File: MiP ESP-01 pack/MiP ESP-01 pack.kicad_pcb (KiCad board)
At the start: 2 copper layers, 41.4 x 63.8 mm, 19 parts, among them J1 MiP, J2 Debug, U1 ESP-01, U2 74LVC1G125, U3 AMS1117-3.3

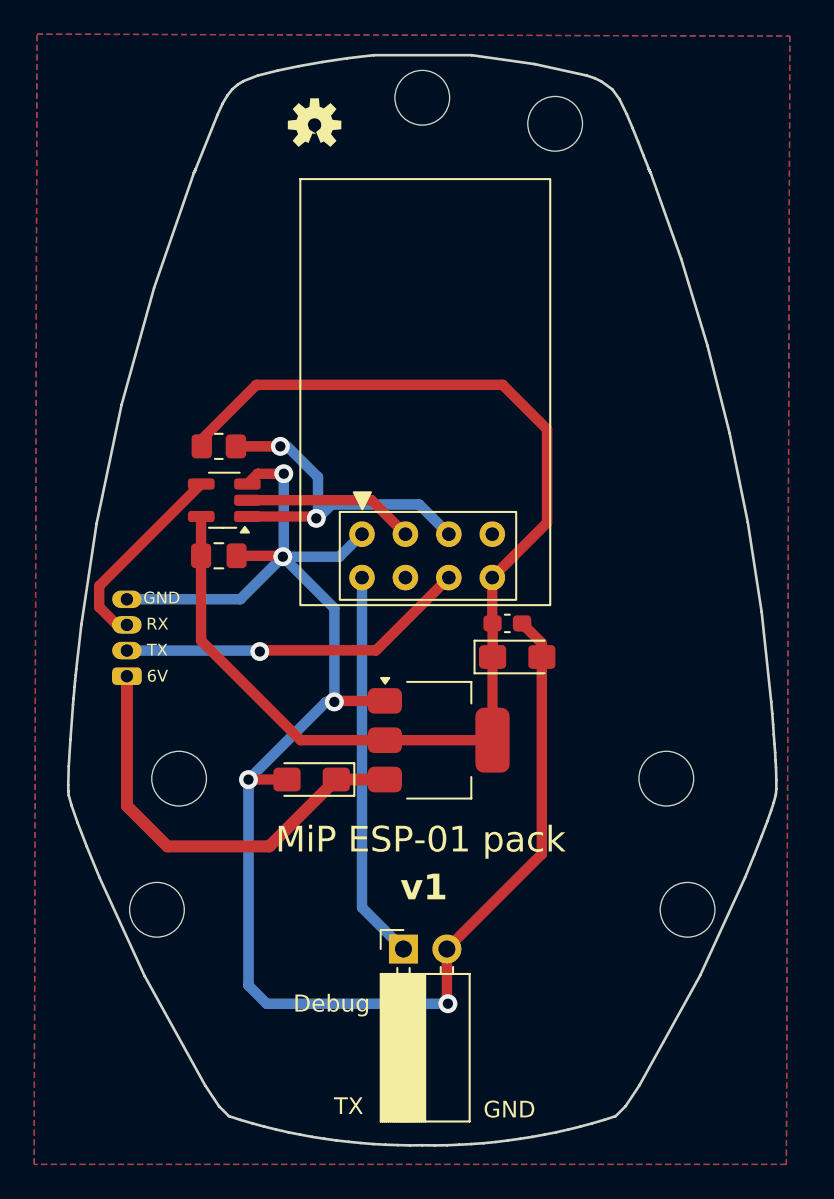
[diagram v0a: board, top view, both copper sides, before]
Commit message: Redoing placement and tracks
Added top and bottom renders too
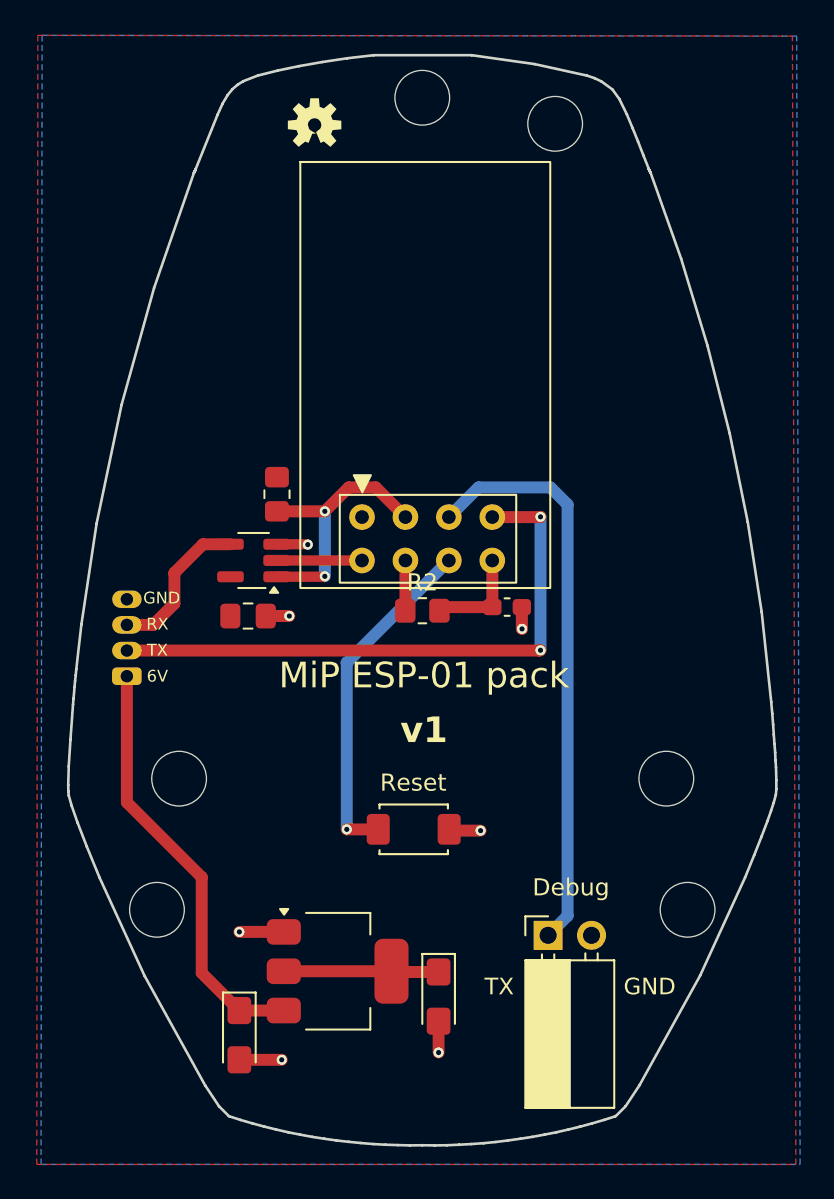
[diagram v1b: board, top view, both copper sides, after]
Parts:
- added R2: 10K, Resistor_SMD:R_0805_2012Metric_Pad1.20x1.40mm_HandSolder, F.Cu at (148.5, 105.6)
- added S1: Reset, PCM_JLCPCB:SW_TS-1088-AR02016, F.Cu at (148.0, 118.4)
- moved C2 20.4 mm to (149.5, 128.2), turned to -90 degrees
- moved C3 15.5 mm to (137.8, 130.4), turned to -90 degrees
- moved U3 14.7 mm to (143.6, 126.7)
- moved J2 8.50 mm to (155.9, 124.6)
- moved R1 4.40 mm to (140.0, 98.8), turned to 90 degrees
- moved C1 3.92 mm to (138.3, 105.9)
- moved U2 3.92 mm to (138.6, 102.7)
- moved U1 1.00 mm to (145.0, 100.1)
- moved C4 0.96 mm to (153.5, 105.4)
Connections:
- R1 pad 1: Net-(U1-Pin_3) -> /BUF_EN
- U1 pad 2: /D1_TX -> /BUF_EN
- U1 pad 3: Net-(U1-Pin_3) -> /Debug
- U1 pad 4: unconnected-(U1-Pin_4-Pad4) -> /RX
- U1 pad 5: /Debug -> /E1_TX
- U1 pad 6: unconnected-(U1-Pin_6-Pad6) -> Net-(U1-Pin_6)
- U1 pad 7: /RX -> Net-(S1-A)
- U2 pad 1: Net-(U1-Pin_3) -> /BUF_EN
- U2 pad 2: /D1_TX -> /E1_TX
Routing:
- net GND: track 96.5 -> 13.2 mm, vias 5 -> 7
- net +3V3: track 69.3 -> 15.0 mm
- net Net-(U1-Pin_3): track 20.4 -> 0.00 mm, vias 2 -> 0
- net Net-(S1-A): track 0.00 -> 20.1 mm, vias 0 -> 1
- net /BUF_EN: track 0.00 -> 15.4 mm, vias 0 -> 2
- net /RX: track 20.5 -> 34.8 mm, vias 1 -> 2
- net /Debug: track 22.7 -> 33.8 mm
- net /D1_TX: track 10.1 -> 0.00 mm
- net /E1_TX: track 0.00 -> 4.99 mm
- net Net-(U1-Pin_6): track 0.00 -> 2.94 mm
- net /BUF_TX: track 11.9 -> 9.13 mm
